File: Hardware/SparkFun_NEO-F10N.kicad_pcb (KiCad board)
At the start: 4 copper layers, 50.8 x 38.1 mm, 94 parts, among them J1 USB_C_Receptacle, J2 Conn_01x09, J5 SMA_EdgeMount, U1 TVS_ESD_USB, U2 AP2112K-3.3, U3 NEO-F10N, U8 CH340C

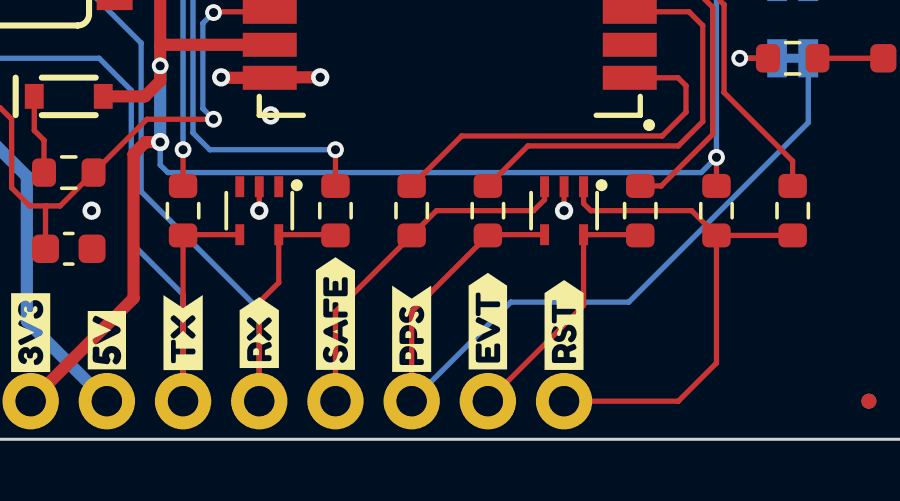
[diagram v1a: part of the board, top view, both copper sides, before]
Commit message: Add bars to RESET and SAFE labels
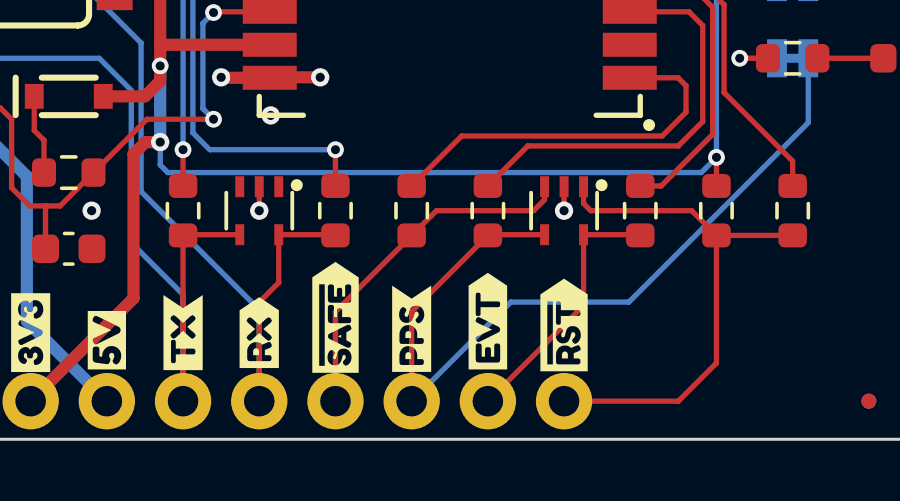
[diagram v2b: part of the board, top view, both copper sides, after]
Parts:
- removed kibuzzard-654D231A: G***, kibuzzard-654D231A
- removed kibuzzard-654D235D: G***, kibuzzard-654D235D
- removed kibuzzard-654D4E4D: G***, kibuzzard-654D4E4D
- removed kibuzzard-654D4E8F: G***, kibuzzard-654D4E8F
- added kibuzzard-655A6C20: G***, kibuzzard-655A6C20, F.Cu at (135.9, 148.6)
- added kibuzzard-655A6C73: G***, kibuzzard-655A6C73, B.Cu at (135.9, 148.0)
- added kibuzzard-655A6CC4: G***, kibuzzard-655A6CC4, F.Cu at (128.3, 148.3)
- added kibuzzard-655A6CE2: G***, kibuzzard-655A6CE2, B.Cu at (128.3, 148.3)

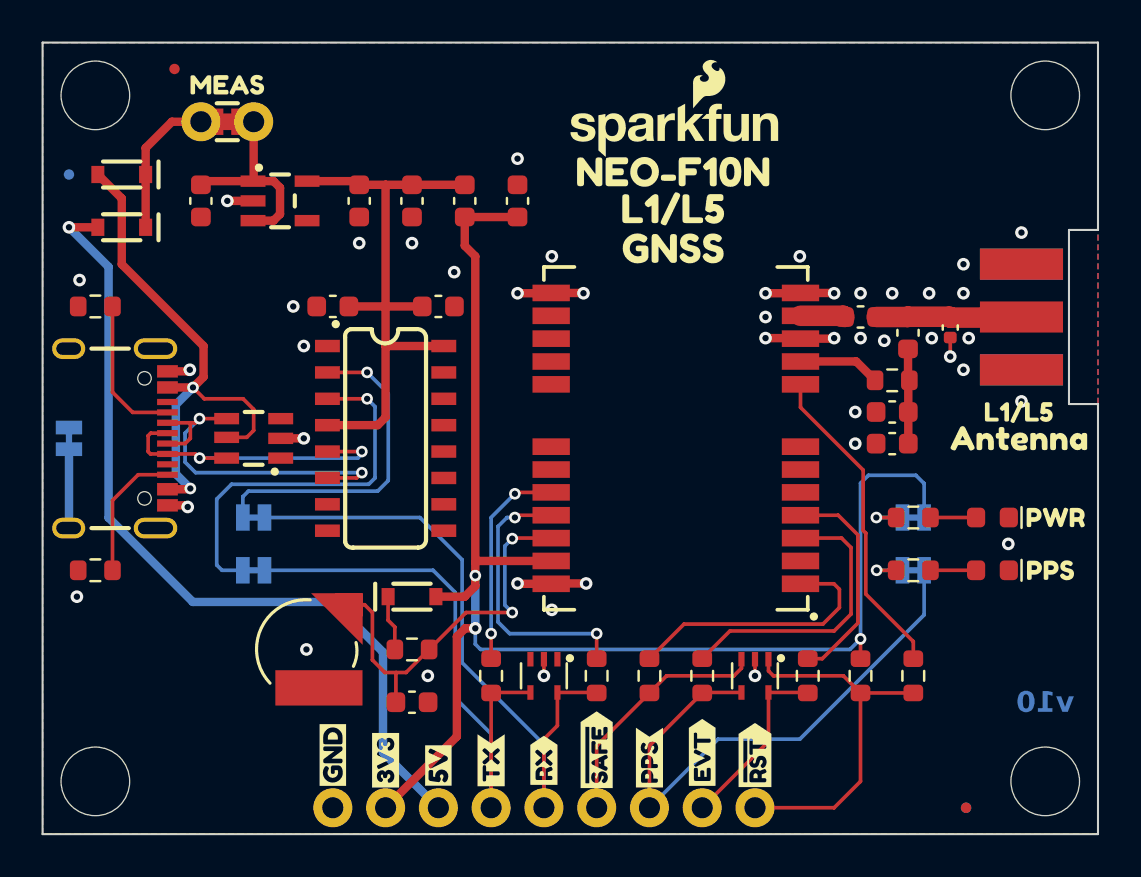
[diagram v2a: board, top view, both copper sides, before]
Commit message: Update layout and panel files post design review.
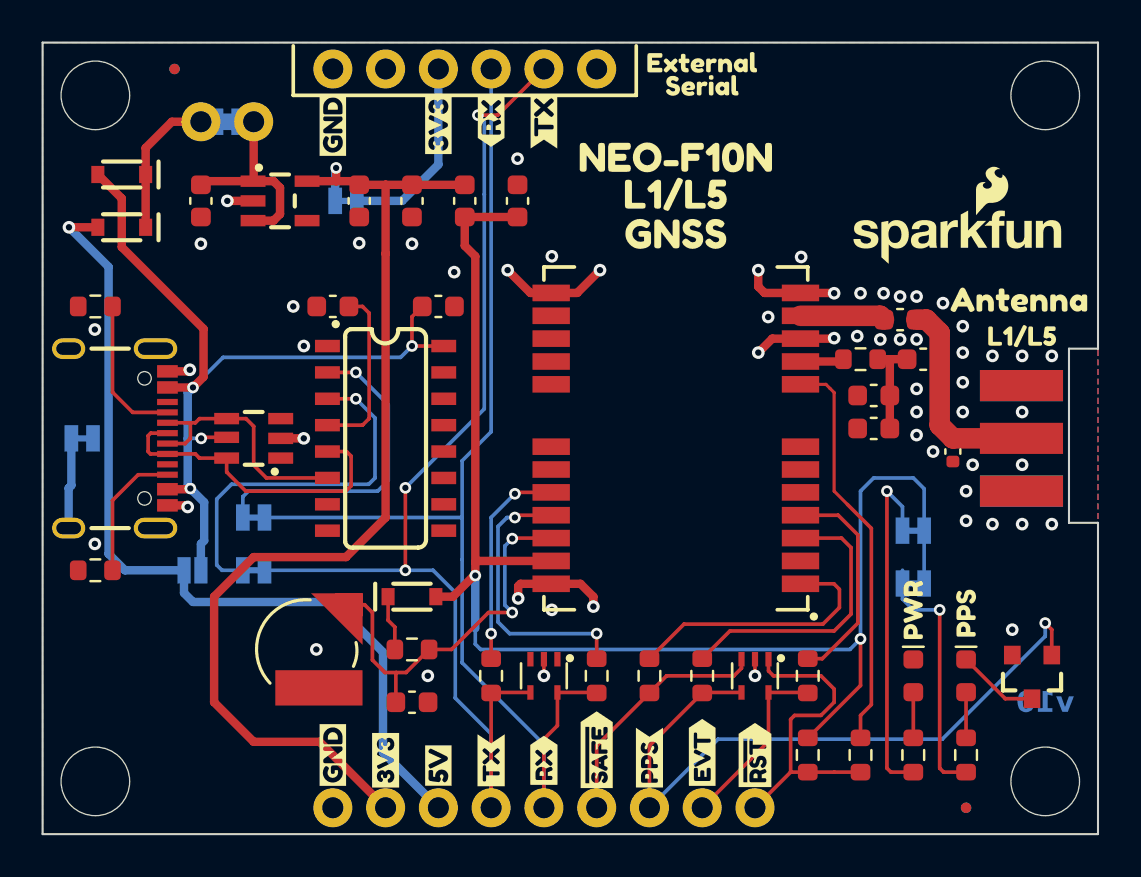
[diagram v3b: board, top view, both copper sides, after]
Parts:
- removed kibuzzard-64C3DF93: G***, kibuzzard-64C3DF93
- removed kibuzzard-64CB1646: G***, kibuzzard-64CB1646
- removed kibuzzard-64CB1658: G***, kibuzzard-64CB1658
- added J4: Conn_01x06, SparkFun-Connector:1X06, F.Cu at (128.3, 115.6)
- added JP6: ~, SparkFun-Jumper:SMT-JUMPER_2_NO_SILK, B.Cu at (108.8, 139.7)
- added JP8: ~, SparkFun-Jumper:SMT-JUMPER_2_NC_TRACE_SILK, B.Cu at (116.2, 121.9)
- added Q1: BSS138, SparkFun-Semiconductor-Standard:SOT23-3, F.Cu at (149.2, 144.8)
- added kibuzzard-64E773DA: G***, kibuzzard-64E773DA, F.Cu at (115.6, 118.3)
- added kibuzzard-64E773DA: G***, kibuzzard-64E773DA, B.Cu at (115.6, 118.3)
- added kibuzzard-659876FC: G***, kibuzzard-659876FC, F.Cu at (123.2, 118.1)
- added kibuzzard-6598770D: G***, kibuzzard-6598770D, F.Cu at (125.7, 118.1)
- added kibuzzard-65989731: G***, kibuzzard-65989731, F.Cu at (120.7, 118.3)
- added kibuzzard-65989731: G***, kibuzzard-65989731, B.Cu at (120.7, 118.3)
- added kibuzzard-65989781: G***, kibuzzard-65989781, B.Cu at (123.2, 118.1)
- added kibuzzard-6598978C: G***, kibuzzard-6598978C, B.Cu at (125.7, 118.1)
- added kibuzzard-65989942: G***, kibuzzard-65989942, F.Cu at (133.3, 115.3)
- added kibuzzard-65989942: G***, kibuzzard-65989942, B.Cu at (133.3, 115.3)
- added kibuzzard-6598994F: G***, kibuzzard-6598994F, F.Cu at (133.3, 116.4)
- added kibuzzard-6598994F: G***, kibuzzard-6598994F, B.Cu at (133.3, 116.4)
- added kibuzzard-65989F3D: G***, kibuzzard-65989F3D, B.Cu at (104.8, 139.7)
- added kibuzzard-65989F89: G***, kibuzzard-65989F89, B.Cu at (140.3, 137.8)
- added kibuzzard-65989F92: G***, kibuzzard-65989F92, B.Cu at (140.5, 140.3)
- added kibuzzard-6598A013: G***, kibuzzard-6598A013, B.Cu at (111.4, 121.9)
- added kibuzzard-6598A076: G***, kibuzzard-6598A076, B.Cu at (107.0, 133.3)
- C12: value 2.2uF -> 0.1uF
- C13: value 100pF -> 0.1uF
- FID1, FID2, FID3, FID4: value Fiducial_0.5 -> Fiducial_0.5mm
- JP5, kibuzzard-654D24CA: moved to B.Cu
- moved G*** 14.6 mm to (145.6, 123.5)
- moved R4 11.4 mm to (143.5, 148.6), turned to 90 degrees
- moved R5 9.25 mm to (146.1, 148.6), turned to 90 degrees
- moved D1 8.52 mm to (143.5, 144.8), turned to -90 degrees
- moved kibuzzard-64C2E6A3 8.17 mm to (143.5, 141.6), turned to 90 degrees
- moved FID2 7.18 mm to (108.0, 115.6)
- moved kibuzzard-64C2EB16 6.67 mm to (148.6, 126.7)
- moved D6 5.97 mm to (145.4, 134.0)
- moved J5 5.84 mm to (148.7, 133.3)
- moved D4 5.24 mm to (146.1, 144.8), turned to -90 degrees
- moved R12 4.58 mm to (138.4, 148.6)
- moved R34 4.58 mm to (141.0, 148.6), turned to 90 degrees
- moved kibuzzard-64C2E6BD 4.56 mm to (146.1, 141.8), turned to 90 degrees
- moved kibuzzard-654D4A62 3.65 mm to (148.7, 128.4)
- moved C7 1.91 mm to (142.9, 127.6)
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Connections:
- net +5V renamed 5V
- C12 pad 1: +3.3V -> VBUS
- C13 pad 1: +3.3V -> 3.3V_P
- C16 pad 1: +3.3V_A -> 3.3V_A
- C2 pad 1: +3.3V -> 3.3V
- C8 pad 1: +3.3V -> 3.3V
- D4 pad 1: GND -> Net-(D4-K)
- D5 pad A: +3.3V_A -> 3.3V_A
- J2 pad 8: +3.3V_A -> 3.3V
- JP2 pad 2: +3.3V_A -> 3.3V_A
- JP3 pad 2: PPS -> 3.3V_A
- L2 pad 1: +3.3V -> 3.3V
- L2 pad 2: +3.3V_A -> 3.3V_A
- R12 pad 1: +3.3V_A -> 3.3V_A
- R34 pad 1: Net-(U3-~{RESET}) -> ~{RESET}
- R34 pad 2: ~{RESET} -> Net-(U3-~{RESET})
- U2 pad 5: +3.3V -> 3.3V
- U3 pad 23: +3.3V_A -> 3.3V_A
- U8 pad 16: +3.3V -> VBUS
- U8 pad 4: +3.3V -> 3.3V_P
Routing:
- net +3.3V_A: track 72.6 -> 0.00 mm, vias 3 -> 0
- net 3.3V_A: track 0.00 -> 68.6 mm, vias 0 -> 2
- net 3.3V: track 0.00 -> 51.2 mm, vias 0 -> 1
- net +3.3V: track 28.1 -> 0.00 mm
- net TXD: track 28.1 -> 55.8 mm, vias 0 -> 3
- net RXD: track 31.6 -> 55.0 mm
- net VBUS: track 26.2 -> 41.1 mm, vias 2 -> 4
- net Net-(JP2-A): track 2.21 -> 16.3 mm
- net Net-(JP3-A): track 2.18 -> 12.4 mm
- net Net-(J4-Pin_4): track 0.00 -> 9.25 mm
- net 3.3V_P: track 0.00 -> 8.32 mm
- net /D-: track 17.8 -> 12.0 mm, vias 2 -> 0
- net PPS: track 27.7 -> 33.3 mm, vias 0 -> 1
- net GND: track 20.1 -> 24.9 mm, vias 44 -> 58
- net Net-(D4-K): track 0.00 -> 3.96 mm
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- removed copper zone on In1.Cu, net GND
- removed copper zone on In2.Cu, net GND
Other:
- outline, holes or cut-outs redrawn
- copper layers 4 -> 2
- board text added: "Finish: HASL Lead-Free"
- board text added: "Layers: 2"
- board text removed: "Controlled Impedance: JLC7628"
- board text removed: "Finish: ENIG"
- board text removed: "Layers: 4"
- board text removed: "No Clean Process"

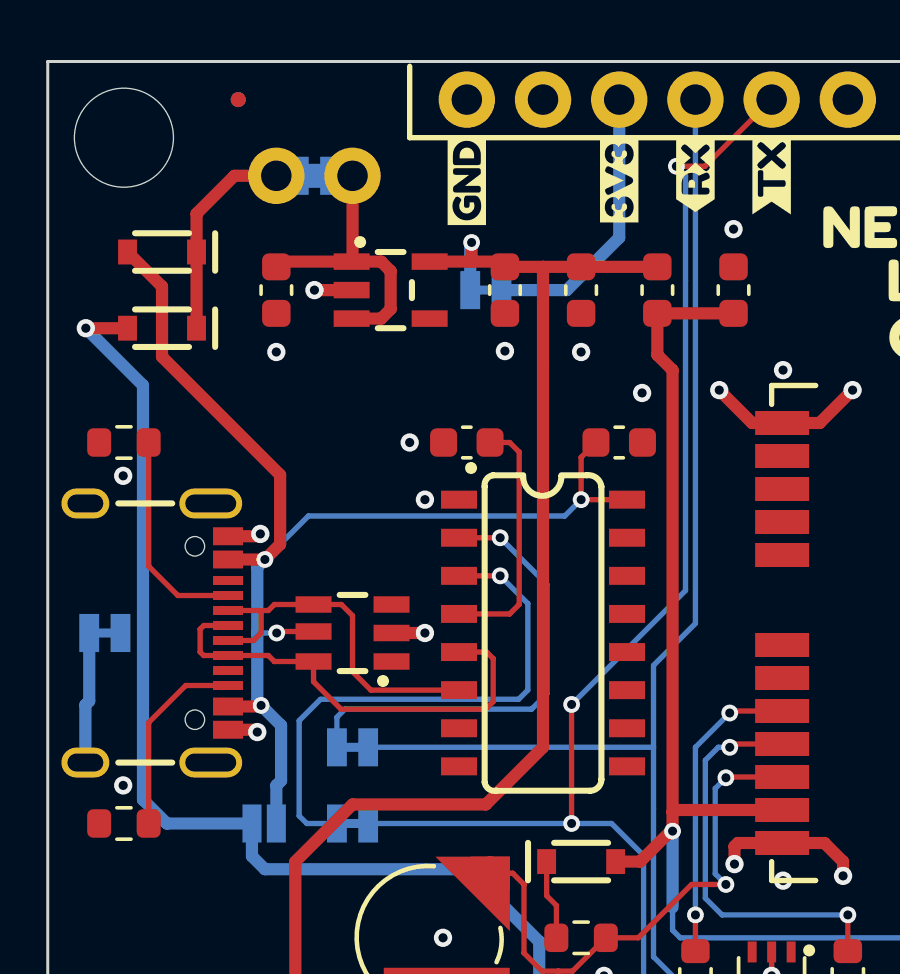
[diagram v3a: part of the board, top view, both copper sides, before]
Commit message: Update 3D models
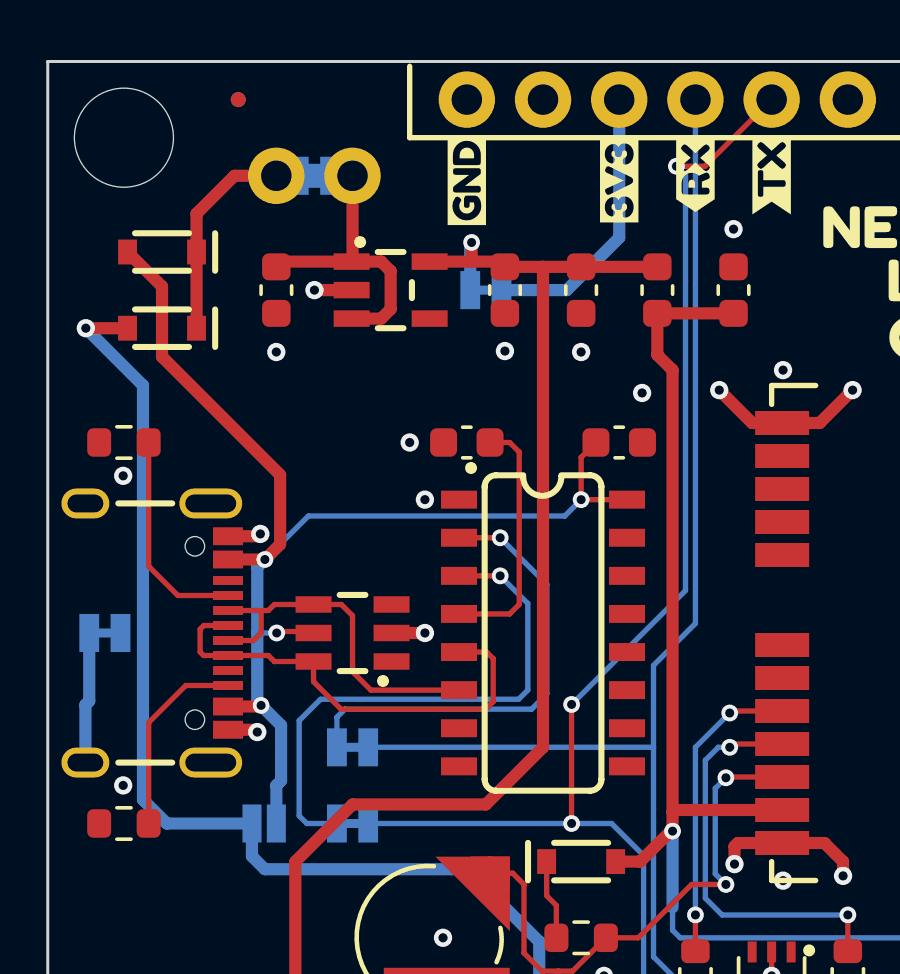
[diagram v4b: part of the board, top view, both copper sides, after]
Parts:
- D1: footprint SparkFun-LED:LED_0603_1608Metric -> SparkFun-LED:LED_0603_1608Metric_Red
- D2, D3: value TVS_ESD_4 -> PESD3V3L4UG
- D4: footprint SparkFun-LED:LED_0603_1608Metric -> SparkFun-LED:LED_0603_1608Metric_Yellow
- D5, D7, D8: value 0.5A -> PMEG4005EJ
- D6: value TVS_0402 -> PESD0402
- J1: footprint SparkFun-Connector:USB-C-16P -> SparkFun-Connector:USB-C_16
- J2: footprint SparkFun-Connector:1X09 -> SparkFun-Connector:1x09
- J4: footprint SparkFun-Connector:1X06 -> SparkFun-Connector:1x06
- J5: value SMA_EdgeMount -> Val**; footprint SparkFun-Connector:SMA-EDGE -> SparkFun-Connector:SMA_Edge
- JP1, JP2, JP3, JP4, JP7, JP8: footprint SparkFun-Jumper:SMT-JUMPER_2_NC_TRACE_SILK -> SparkFun-Jumper:Jumper_2_NC_Trace
- JP5: footprint SparkFun-Jumper:COMBO-JUMPER_2_NC_TRACE -> SparkFun-Jumper:Jumper_2_PTH_SMD_Combo-NC
- JP6: footprint SparkFun-Jumper:SMT-JUMPER_2_NO_SILK -> SparkFun-Jumper:Jumper_2_NO
- ST1, ST2, ST3, ST4: value Stand_off -> STAND-OFF; footprint SparkFun-Hardware:STAND-OFF -> SparkFun-Hardware:Standoff
- U1: value TVS_ESD_USB -> DT1042-04SO
- U7: footprint SparkFun-Aesthetic:ORDERING_INSTRUCTIONS -> SparkFun-Aesthetic:Ordering_Instructions
- U8: footprint SparkFun-Semiconductor-Standard:SO16 -> SparkFun-Semiconductor-Standard:SO-16
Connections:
- J5 pad 1: GND -> Net-(D6-A2)
